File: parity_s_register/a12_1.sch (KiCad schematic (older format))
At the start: 33 parts, among them U12001 74HC04, U12002 74HC27, U12003 74HC27, U12004 74HC4002, U12005 74HC04, U12006 74HC27, U12007 74HC27, U12008 74HC4002, U12009 74HC04, U12010 74HC27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

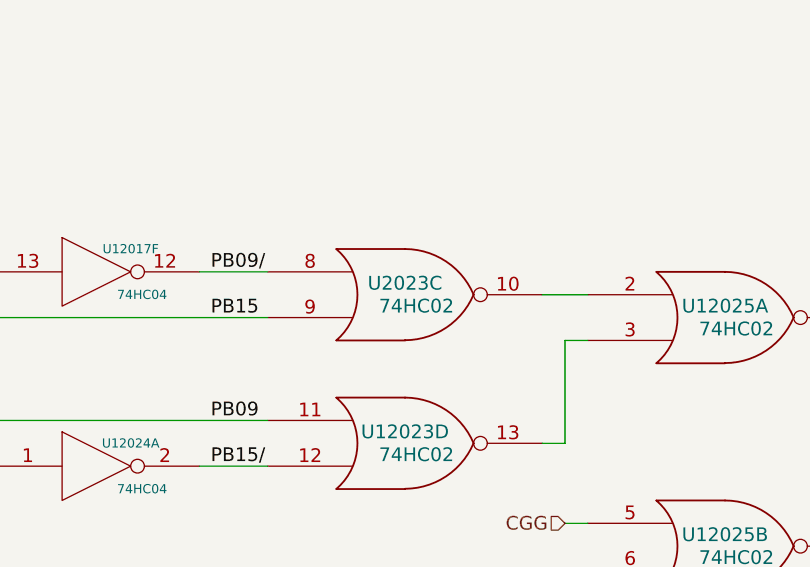
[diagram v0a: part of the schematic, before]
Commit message: Bux fixes for things found during FPGA integration.
* A05 was driving TSGN/ directly instead of with an OD buffer+pullup
* Some bad logic with crosspoints in module 5
* A bad part number in module 12
* Removal of unused signals from the backplane connectors
* Addition of some monitor signals from the timer to the backplane
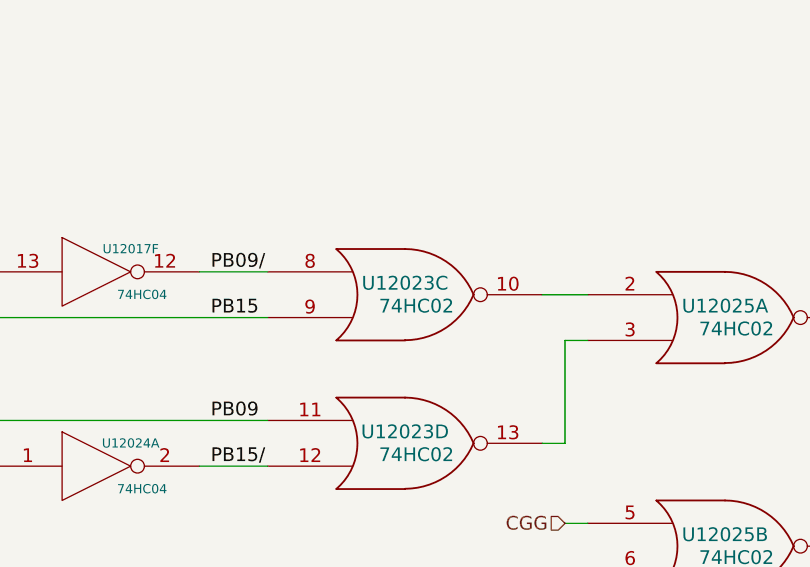
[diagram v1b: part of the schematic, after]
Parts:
- renumbered U2023 to U12023
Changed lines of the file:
@@
 	12250 11350 12500 11350
 $Comp
-L 74HC02 U2023
+L 74HC02 U12023
 U 3 1 56B57830
 P 14300 10600
-F 0 "U2023" H 14300 10650 60  0000 C CNN
+F 0 "U12023" H 14300 10650 60  0000 C CNN
 F 1 "74HC02" H 14350 10550 60  0000 C CNN
 F 2 "" H 14300 10600 60  0000 C CNN

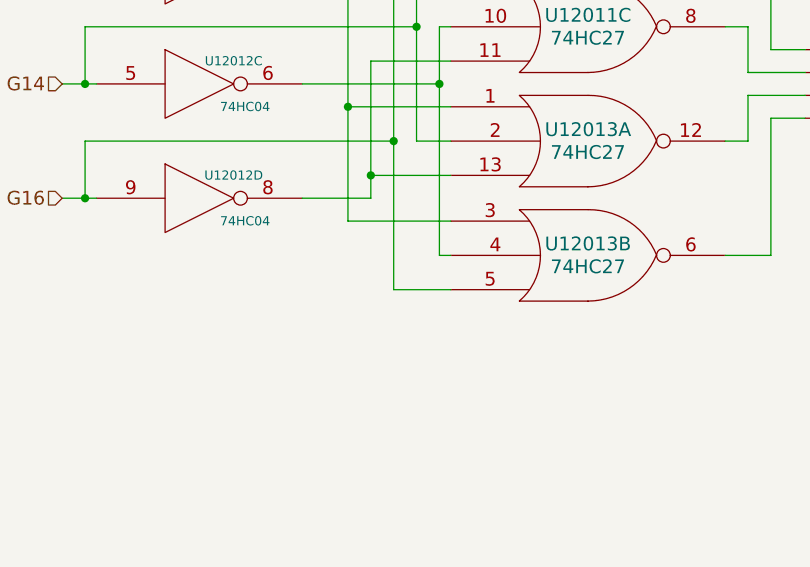
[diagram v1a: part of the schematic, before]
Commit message: Added erasable memory, and fixed lots of random wiring errors.
I decided to go with a 16-bit-wide MRAM chip -- I had  no idea
until I started researching RAM options how technologically
similar MRAM is to core memory. The datasheet diagrams look like
they're straight out of the AGC documentation!

There's a slight inaccuracy in this implementation worth mentioning.
Like fixed memory, I've wired the sense amplifier outputs directly up
to the tristate data output pins of the MRAM chip. But because the
data lines are bidirectional, data being written into RAM will show up
on the sense lines, and go straight into the ungated G register. Since
G is what's being written out, this doesn't matter 99% of the time, but
if there's an overflow condition in G (I don't even know if this is
possible), the bit 16 will be copied over bit 16, and the overflow
condition will be lost. I'll keep an eye out to see if anything relies
on G not changing after the write cycle is complete.

With erasable memory introduced, the computer now theoretically supports
all programs that don't use I/O or interrupts. I've started running
the VirtualAGC validation program, and have been fixing random errors
uncovered by failing self-tests.
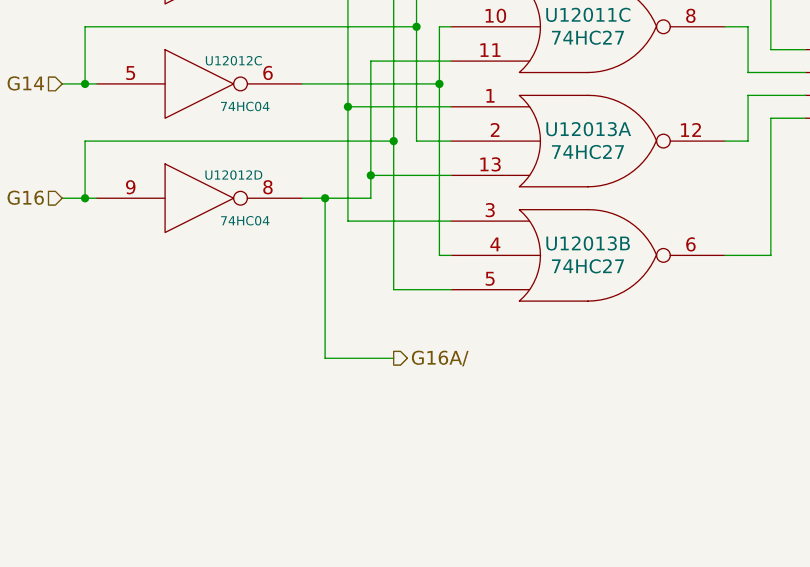
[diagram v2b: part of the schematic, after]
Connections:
- net G16A/: now reaches U12011.11, U12012.8, U12013.13
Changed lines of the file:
@@
 Text Label 11250 5350 0    60   ~ 0
 T7PHS4/
+Wire Wire Line
+	2200 10450 2200 11150
+Wire Wire Line
+	2200 11150 2500 11150
+Connection ~ 2200 10450
+Text HLabel 2500 11150 2    60   Output ~ 0
+G16A/
 $EndSCHEMATC

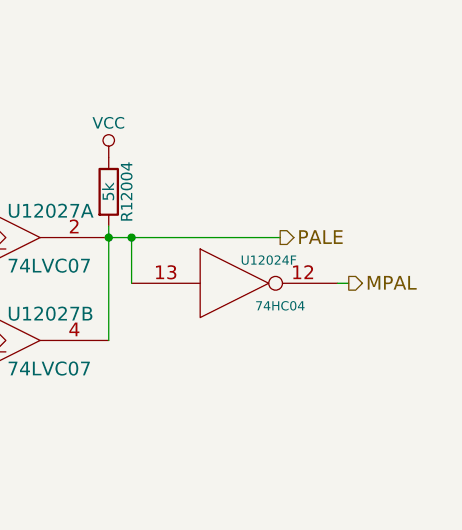
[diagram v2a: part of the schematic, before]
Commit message: Broke all the monitor outputs I could find out to the backplane, in preparation for making a monitor
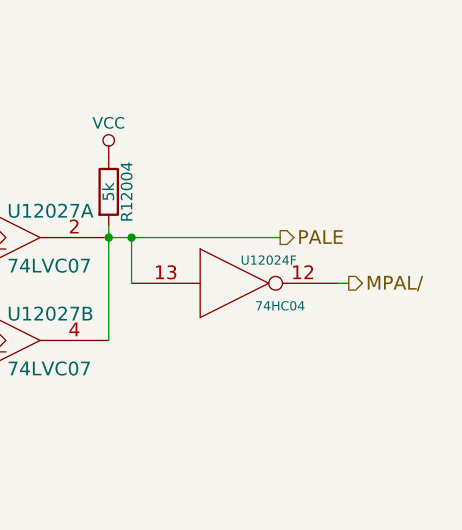
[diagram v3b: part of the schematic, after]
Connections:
- net MPAL renamed MPAL/
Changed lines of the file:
@@
 	22250 11800 22300 11800
 Text HLabel 22300 11800 2    60   Output ~ 0
-MPAL
+MPAL/
 $Comp
 L 74HC27 U12026

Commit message: Fixed not->1-input nor in the rest of the modules.
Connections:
- wire segments 389 -> 394
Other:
- note removed: "This input was cut off in the originals. It *might* apply \nto T7PHS4/ rather than T7PHS4. Needs testing."
- moved on the sheet: R12001, R12004, U12001A, U12001B, U12001C, U12001D, U12001E, U12001F, U12005A, U12005B, U12005C, U12005D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

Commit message: Updated Parity and S Register to be on +4VSW
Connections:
- net labels added: +4VSW
- net labels removed: VCC

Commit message: Some initial condition updates for the CH77 alarm box and a monitor output I missed converting to 74LVC06
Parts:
- removed unit 6 of U12024
- added U12050: 74LVC06, symbol 74LVC06
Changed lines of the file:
@@
 LIBS:contrib
 LIBS:valves
-LIBS:parity_s_register-cache
-EELAYER 25 0
+EELAYER 26 0
 EELAYER END
 $Descr A2 23386 16535
@@
 Text HLabel 21700 11600 2    60   Output ~ 0
 PALE
-$Comp
-L 74HC04 U12024
-U 6 1 56B9BAB9
-P 21700 11900
-AR Path="/56B9BAB9" Ref="U12024"  Part="6"
-AR Path="/56ADAA5B/56B9BAB9" Ref="U12024"  Part="6"
-F 0 "U12024" H 21700 11950 60  0000 C CNN
-F 1 "74HC04" H 21700 11650 60  0001 C CNN
-F 2 "" H 21700 11900 60  0000 C CNN
-F 3 "" H 21700 11900 60  0000 C CNN
-	6    21700 11900
-	1    0    0    -1
-$EndComp
 Wire Wire Line
 	21050 11900 21050 11600
 Connection ~ 21050 11600
 Wire Wire Line
-	22300 11900 22350 11900
-Text HLabel 22350 11900 2    60   Output ~ 0
+	22000 11900 22050 11900
+Text HLabel 22050 11900 2    60   Output ~ 0
 MPAL/
 $Comp
@@
 	1    0    0    -1
 $EndComp
+$Comp
+L 74LVC06 U12050
+U 1 1 58D8F248
+P 21550 11900
+F 0 "U12050" H 21550 11700 60  0000 C CNN
+F 1 "74LVC06" H 21550 11850 60  0001 C CNN
+F 2 "" H 21550 11900 60  0000 C CNN
+F 3 "" H 21550 11900 60  0000 C CNN
+	1    21550 11900
+	1    0    0    -1
+$EndComp

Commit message: This adds fixes to the schematics for changes identified in comparing against the independent AGC schematics in the "schematics" branch of the main Virtual AGC repository.  Changes include:  Topological (but not logical) fixes to the DKCTR4,5,4/,5/ signals in the inout_v schematic. Wiring fix (incorrect signal sources for 5 gates) in inout_iv. Fixed incorrect signal source (including MGOJAM output polarity) for one gate in timer.  Fixed incorrect topology (but not logic) for 3 output signals in service_gates. Fixed backplane signal source (MYCLMP incorrectly used everywhere in place of the correct STRT2) in memory_timing_addressing.  ROPER, ROPES, ROPET had incorrectly omitted STRT2 as an input signal in four_bit_2. A couple of  internal nets local to sheets were also renamed due to conflicts with analysis software.  None of these fixes had any measurable effect on instruction execution; Validation was passed prior to the fixes, and continues to be passed after the fixes, and the identical instruction sequence occurs in doing so.
For me, warnings about missing components from the libraries occur upon every schematic load, though
these missing components don't seem to actually be in the circuits.  I tried to make some library
changes to work around that.  My changes don't actually fix the problem, but rather than try to back
them out and redo all the testing, they're a part of this commit as well.
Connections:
- net labels added: uG02/, uG03/
- net labels removed: G02/, G03/
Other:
- moved on the sheet: U12001B, U12001C
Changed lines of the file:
@@
 LIBS:contrib
 LIBS:valves
+LIBS:parity_s_register-cache
 EELAYER 26 0
 EELAYER END
@@
 L 74HC04 U12001
 U 2 1 56ADACA5
-P 1500 1550
+P 1400 1550
 AR Path="/56ADACA5" Ref="U12001"  Part="2"
 AR Path="/56ADAA5B/56ADACA5" Ref="U12001"  Part="2"
-F 0 "U12001" H 1500 1600 60  0000 C CNN
-F 1 "74HC04" H 1500 1300 60  0001 C CNN
-F 2 "" H 1500 1550 60  0000 C CNN
-F 3 "" H 1500 1550 60  0000 C CNN
-	2    1500 1550
+F 0 "U12001" H 1400 1600 60  0000 C CNN
+F 1 "74HC04" H 1400 1300 60  0001 C CNN
+F 2 "" H 1400 1550 60  0000 C CNN
+F 3 "" H 1400 1550 60  0000 C CNN
+	2    1400 1550
 	1    0    0    -1
 $EndComp
@@
 L 74HC04 U12001
 U 3 1 56ADAD82
-P 1500 2050
+P 1400 2050
 AR Path="/56ADAD82" Ref="U12001"  Part="3"
 AR Path="/56ADAA5B/56ADAD82" Ref="U12001"  Part="3"
-F 0 "U12001" H 1500 2100 60  0000 C CNN
-F 1 "74HC04" H 1500 1800 60  0001 C CNN
-F 2 "" H 1500 2050 60  0000 C CNN
-F 3 "" H 1500 2050 60  0000 C CNN
-	3    1500 2050
+F 0 "U12001" H 1400 2100 60  0000 C CNN
+F 1 "74HC04" H 1400 1800 60  0001 C CNN
+F 2 "" H 1400 2050 60  0000 C CNN
+F 3 "" H 1400 2050 60  0000 C CNN
+	3    1400 2050
 	1    0    0    -1
 $EndComp
@@
 Text HLabel 11300 4500 0    60   Input ~ 0
 TSUDO/
-Text Label 2250 2050 2    60   ~ 0
-G03/
-Text Label 2250 1550 2    60   ~ 0
-G02/
+Text Label 2000 2050 0    60   ~ 0
+uG03/
+Text Label 2000 1550 0    60   ~ 0
+uG02/
 Text HLabel 2200 850  2    60   Output ~ 0
 G01A/
@@
 G01A/
 Text Label 13300 5500 0    60   ~ 0
-G02/
+uG02/
 Text Label 13300 5700 0    60   ~ 0
 G03
@@
 	750  1050 900  1050
 Wire Wire Line
-	750  1550 900  1550
-Wire Wire Line
-	750  2050 900  2050
+	750  1550 850  1550
+Wire Wire Line
+	750  2050 850  2050
 Wire Wire Line
 	2100 1050 2300 1050
@@
 Connection ~ 2300 1650
 Wire Wire Line
-	2400 2050 2100 2050
+	2400 2050 2000 2050
 Wire Wire Line
 	2400 1450 2400 2050
@@
 	2300 2150 2750 2150
 Wire Wire Line
-	850  2050 850  1800
-Wire Wire Line
-	850  1800 2500 1800
+	800  2050 800  1800
+Wire Wire Line
+	800  1800 2500 1800
 Wire Wire Line
 	2500 950  2500 2450
 Wire Wire Line
 	2500 2450 2750 2450
-Connection ~ 850  2050
+Connection ~ 800  2050
 Wire Wire Line
 	2500 950  2750 950
 Connection ~ 2500 1800
 Wire Wire Line
-	850  1550 850  1300
-Wire Wire Line
-	850  1300 2600 1300
+	800  1550 800  1300
+Wire Wire Line
+	800  1300 2600 1300
 Wire Wire Line
 	2600 800  2600 1800
 Wire Wire Line
 	2600 800  2750 800
-Connection ~ 850  1550
+Connection ~ 800  1550
 Wire Wire Line
 	2600 1800 2750 1800
@@
 Connection ~ 2700 650
 Wire Wire Line
-	2100 1550 2700 1550
+	2000 1550 2700 1550
 Wire Wire Line
 	2700 1300 2700 2300
@@
 	14150 6900 13300 6900
 Text Label 13300 6900 0    60   ~ 0
-G03/
+uG03/
 $Comp
 L 74HC4002 U12019
@@
 	21050 11900 21100 11900
 $Comp
-L +4VSW #PWR05
+L +4VSW #PWR011
 U 1 1 5812DDE7
 P 10650 3800
-F 0 "#PWR05" H 10650 3650 50  0001 C CNN
+F 0 "#PWR011" H 10650 3650 50  0001 C CNN
 F 1 "+4VSW" H 10650 3940 50  0000 C CNN
 F 2 "" H 10650 3800 60  0000 C CNN
@@
 $EndComp
 $Comp
-L +4VSW #PWR06
+L +4VSW #PWR012
 U 1 1 5812E009
 P 16250 4800
-F 0 "#PWR06" H 16250 4650 50  0001 C CNN
+F 0 "#PWR012" H 16250 4650 50  0001 C CNN
 F 1 "+4VSW" H 16250 4940 50  0000 C CNN
 F 2 "" H 16250 4800 60  0000 C CNN
@@
 $EndComp
 $Comp
-L +4VSW #PWR07
+L +4VSW #PWR013
 U 1 1 5812E98D
 P 16250 6000
-F 0 "#PWR07" H 16250 5850 50  0001 C CNN
+F 0 "#PWR013" H 16250 5850 50  0001 C CNN
 F 1 "+4VSW" H 16250 6140 50  0000 C CNN
 F 2 "" H 16250 6000 60  0000 C CNN
@@
 $EndComp
 $Comp
-L +4VSW #PWR08
+L +4VSW #PWR014
 U 1 1 5812EBAF
 P 20950 11250
-F 0 "#PWR08" H 20950 11100 50  0001 C CNN
+F 0 "#PWR014" H 20950 11100 50  0001 C CNN
 F 1 "+4VSW" H 20950 11390 50  0000 C CNN
 F 2 "" H 20950 11250 60  0000 C CNN
